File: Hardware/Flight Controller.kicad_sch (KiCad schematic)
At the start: 170 parts, among them J1 USB4110GFA, J2 ST_LINK, J3 4in1 ESC, J4 FPV, J5 GPS, J6 RC Receiver, Q1 AO3407A, SW1 reset, SW2 SSSS810701, U1 TPS54302, U10 W25Q128JVSIQ, U11 STM32H743VITx, U12 BMI270, U2 AP63205WU, U3 AZ1117-3.3, U4 USBLC6-2SC6, U5 AT7456E, U6 INA226, U7 ICM-42688-P, U8 QMC5883P, U9 BMP388, Y1 27Mhz 20pF, Y2 8MHz 12pF

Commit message: Added connectors STEP files, edited Schematics and started layout
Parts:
- added C15: 0.1uF, Capacitor_SMD:C_0402_1005Metric, symbol Device:C_Small
- C7: footprint Capacitor_SMD:C_0603_1608Metric -> Capacitor_SMD:C_0805_2012Metric
- J2: footprint Connector_PinHeader_2.54mm:PinHeader_1x04_P2.54mm_Horizontal -> memo:CONN-SMD_4P-P1.00_SM04B-SRSS-TB-LF-SN
- J4: footprint Connector_JST:JST_SH_SM04B-SRSS-TB_1x04-1MP_P1.00mm_Horizontal -> memo:CONN-SMD_4P-P1.00_SM04B-SRSS-TB-LF-SN
- J6: footprint Connector_JST:JST_GH_SM04B-GHS-TB_1x04-1MP_P1.25mm_Horizontal -> memo:CONN-SMD_4P-P1.00_SM04B-SRSS-TB-LF-SN
- R7: value 1k -> 330
- TP21, TP26: footprint Solderpoint:Solderpad -> Solderpoint:BAT pad
- renumbered C15 to C16, C16 to C17, C17 to C18, C18 to C19, C19 to C20, C20 to C21, C21 to C22, C22 to C23, C23 to C24, C24 to C25, C25 to C26, C26 to C27, C27 to C28, C28 to C29, C29 to C30, C30 to C31, C31 to C32, C32 to C33, C33 to C34, C34 to C35, C35 to C36, C36 to C37, C37 to C38, C38 to C39, C39 to C40, C40 to C41, C41 to C42, C42 to C43, C43 to C44, C44 to C45, C45 to C46, C46 to C47, C47 to C48, C48 to C49, C49 to C50, C50 to C51, C51 to C52, C52 to C53, C53 to C54, C54 to C55, C55 to C56
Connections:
- net +5V_USB: now also C15.1
- net GND: now also C15.2
- net A5: now reaches J1.A5 (CC1), R1.2
- net B5: now reaches J1.B5 (CC2), R2.2
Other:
- moved on the sheet: R7

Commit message: This commits updates BOM for Test Board, Changes the Ferrit bead value
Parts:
- FB1: value 120r @ 100KHz -> 1k@100Mhz
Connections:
- net M5: now also J3.6 (Pin_6); no longer J3.3 (Pin_3)
- net M6: now also J3.5 (Pin_5); no longer J3.4 (Pin_4)
- net M7: now also J3.4 (Pin_4); no longer J3.5 (Pin_5)
- net M8: now also J3.3 (Pin_3); no longer J3.6 (Pin_6)
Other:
- moved on the sheet: C13, C14
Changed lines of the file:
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@@
 	(wire
 		(pts
-			(xy 105.41 157.48) (xy 105.41 163.83)
+			(xy 105.41 157.48) (xy 105.41 161.29)
 		)
 		(stroke
@@
 	(wire
 		(pts
-			(xy 110.49 157.48) (xy 110.49 163.83)
+			(xy 110.49 157.48) (xy 110.49 161.29)
 		)
 		(stroke
@@
 	(wire
 		(pts
-			(xy 110.49 168.91) (xy 110.49 171.45)
+			(xy 110.49 166.37) (xy 110.49 171.45)
 		)
 		(stroke
@@
 	(wire
 		(pts
-			(xy 105.41 168.91) (xy 105.41 171.45)
+			(xy 105.41 166.37) (xy 105.41 171.45)
 		)
 		(stroke
@@
 		)
 	)
+	(label "FB_5V"
+		(at 91.44 160.02 0)
+		(effects
+			(font
+				(size 0.762 0.762)
+			)
+			(justify left bottom)
+		)
+	)
 	(label "reset"
 		(at 163.83 210.82 0)
@@
 		)
 	)
-	(global_label "QMC_SDA"
+	(global_label "M8"
 		(shape input)
-		(at 284.48 212.09 270)
+		(at 605.79 181.61 0)
 		(fields_autoplaced yes)
 		(effects
 			(font
 				(size 0.762 0.762)
+				(thickness 0.1524)
+				(bold yes)
 			)
-			(justify right)
+			(justify left)
 		)
 		(property "Intersheetrefs" "${INTERSHEET_REFS}"
-			(at 284.48 219.034 90)
+			(at 609.4635 181.61 0)
 			(effects
 				(font
 					(size 1.27 1.27)
 				)
-				(justify right)
+				(justify left)
 				(hide yes)
 			)
 		)
 	)
-	(global_label "M7"
+	(global_label "QMC_SDA"
 		(shape input)
-		(at 605.79 186.69 0)
+		(at 284.48 212.09 270)
 		(fields_autoplaced yes)
 		(effects
 			(font
 				(size 0.762 0.762)
-				(thickness 0.1524)
-				(bold yes)
 			)
-			(justify left)
+			(justify right)
 		)
 		(property "Intersheetrefs" "${INTERSHEET_REFS}"
-			(at 609.4635 186.69 0)
+			(at 284.48 219.034 90)
 			(effects
 				(font
 					(size 1.27 1.27)
 				)
-				(justify left)
+				(justify right)
 				(hide yes)
 			)
@@
 		)
 	)
-	(global_label "M5"
-		(shape input)
-		(at 605.79 181.61 0)
-		(fields_autoplaced yes)
-		(effects
-			(font
-				(size 0.762 0.762)
-				(thickness 0.1524)
-				(bold yes)
-			)
-			(justify left)
-		)
-		(property "Intersheetrefs" "${INTERSHEET_REFS}"
-			(at 609.4635 181.61 0)
-			(effects
-				(font
-					(size 1.27 1.27)
-				)
-				(justify left)
-				(hide yes)
-			)
-		)
-	)
 	(global_label "WIFI/RC_TX"
 		(shape input)
@@
 		)
 	)
+	(global_label "M6"
+		(shape input)
+		(at 605.79 186.69 0)
+		(fields_autoplaced yes)
+		(effects
+			(font
+				(size 0.762 0.762)
+				(thickness 0.1524)
+				(bold yes)
+			)
+			(justify left)
+		)
+		(property "Intersheetrefs" "${INTERSHEET_REFS}"
+			(at 609.4635 186.69 0)
+			(effects
+				(font
+					(size 1.27 1.27)
+				)
+				(justify left)
+				(hide yes)
+			)
+		)
+	)
+	(global_label "M7"
+		(shape input)
+		(at 605.79 184.15 0)
+		(fields_autoplaced yes)
+		(effects
+			(font
+				(size 0.762 0.762)
+				(thickness 0.1524)
+				(bold yes)
+			)
+			(justify left)
+		)
+		(property "Intersheetrefs" "${INTERSHEET_REFS}"
+			(at 609.4635 184.15 0)
+			(effects
+				(font
+					(size 1.27 1.27)
+				)
+				(justify left)
+				(hide yes)
+			)
+		)
+	)
 	(global_label "NRST"
 		(shape input)
@@
 		)
 	)
-	(global_label "M8"
-		(shape input)
-		(at 605.79 189.23 0)
-		(fields_autoplaced yes)
-		(effects
-			(font
-				(size 0.762 0.762)
-				(thickness 0.1524)
-				(bold yes)
-			)
-			(justify left)
-		)
-		(property "Intersheetrefs" "${INTERSHEET_REFS}"
-			(at 609.4635 189.23 0)
-			(effects
-				(font
-					(size 1.27 1.27)
-				)
-				(justify left)
-				(hide yes)
-			)
-		)
-	)
 	(global_label "ST_SWCLK"
 		(shape input)
@@
 		)
 	)
-	(global_label "M6"
-		(shape input)
-		(at 605.79 184.15 0)
-		(fields_autoplaced yes)
-		(effects
-			(font
-				(size 0.762 0.762)
-				(thickness 0.1524)
-				(bold yes)
-			)
-			(justify left)
-		)
-		(property "Intersheetrefs" "${INTERSHEET_REFS}"
-			(at 609.4635 184.15 0)
-			(effects
-				(font
-					(size 1.27 1.27)
-				)
-				(justify left)
-				(hide yes)
-			)
-		)
-	)
 	(global_label "GPS_TX"
 		(shape input)
@@
 		)
 	)
+	(global_label "M5"
+		(shape input)
+		(at 605.79 189.23 0)
+		(fields_autoplaced yes)
+		(effects
+			(font
+				(size 0.762 0.762)
+				(thickness 0.1524)
+				(bold yes)
+			)
+			(justify left)
+		)
+		(property "Intersheetrefs" "${INTERSHEET_REFS}"
+			(at 609.4635 189.23 0)
+			(effects
+				(font
+					(size 1.27 1.27)
+				)
+				(justify left)
+				(hide yes)
+			)
+		)
+	)
 	(global_label "INA226_ALERT"
 		(shape input)
@@
 	(symbol
 		(lib_id "Device:C_Small")
-		(at 110.49 166.37 180)
+		(at 110.49 163.83 180)
 		(unit 1)
 		(exclude_from_sim no)
@@
 		(dnp no)
 		(property "Reference" "C14"
-			(at 112.268 162.306 0)
+			(at 112.268 159.766 0)
 			(effects
 				(font
@@
 		)
 		(property "Value" "22uF"
-			(at 112.268 164.846 0)
+			(at 112.268 162.306 0)
 			(effects
 				(font
@@
 		)
 		(property "Footprint" "Capacitor_SMD:C_0603_1608Metric"
-			(at 110.49 166.37 0)
+			(at 110.49 163.83 0)
 			(effects
 				(font
@@
 		)
 		(property "Datasheet" "~"
-			(at 110.49 166.37 0)
+			(at 110.49 163.83 0)
 			(effects
 				(font
@@
 		)
 		(property "Description" "Unpolarized capacitor, small symbol"
-			(at 110.49 166.37 0)
+			(at 110.49 163.83 0)
 			(effects
 				(font
@@
 			)
 		)
-		(property "Value" "120r @ 100KHz"
+		(property "Value" "1k@100Mhz"
 			(at 480.0219 86.36 90)
 			(effects
@@
 	(symbol
 		(lib_id "Device:C_Small")
-		(at 105.41 166.37 180)
+		(at 105.41 163.83 180)
 		(unit 1)
 		(exclude_from_sim no)
@@
 		(dnp no)
 		(property "Reference" "C13"
-			(at 99.822 162.306 0)
+			(at 99.822 159.766 0)
 			(effects
 				(font
@@
 		)
 		(property "Value" "22uF"
-			(at 99.822 164.846 0)
+			(at 99.822 162.306 0)
 			(effects
 				(font
@@
 		)
 		(property "Footprint" "Capacitor_SMD:C_0603_1608Metric"
-			(at 105.41 166.37 0)
+			(at 105.41 163.83 0)
 			(effects
 				(font
@@
 		)
 		(property "Datasheet" "~"
-			(at 105.41 166.37 0)
+			(at 105.41 163.83 0)
 			(effects
 				(font
@@
 		)
 		(property "Description" "Unpolarized capacitor, small symbol"
-			(at 105.41 166.37 0)
+			(at 105.41 163.83 0)
 			(effects
 				(font

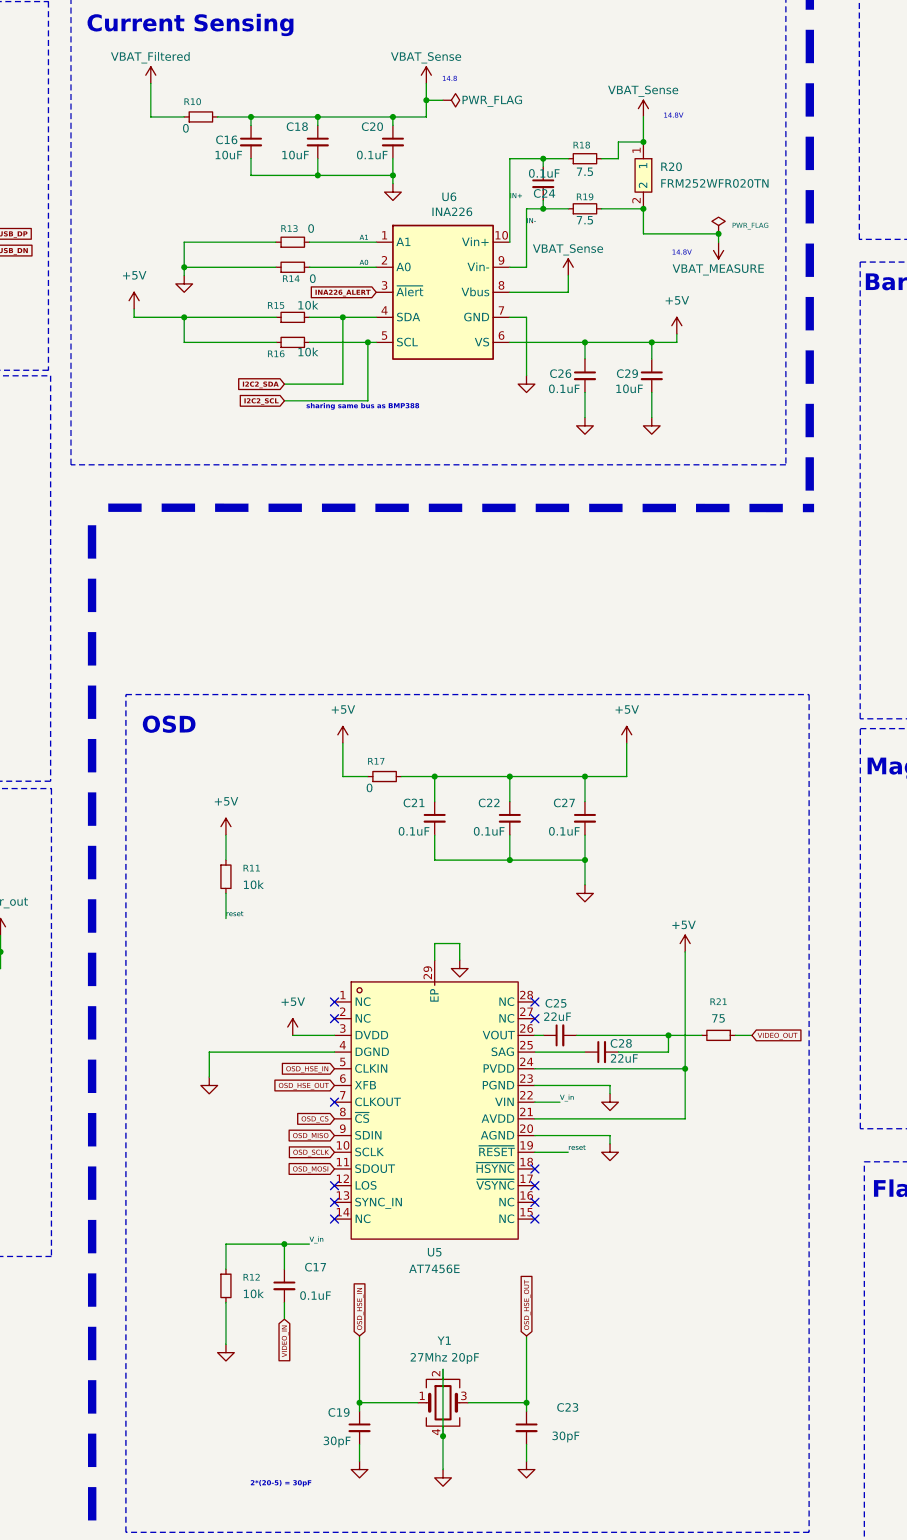
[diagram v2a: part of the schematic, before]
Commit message: Fixed Peripherals for OSD
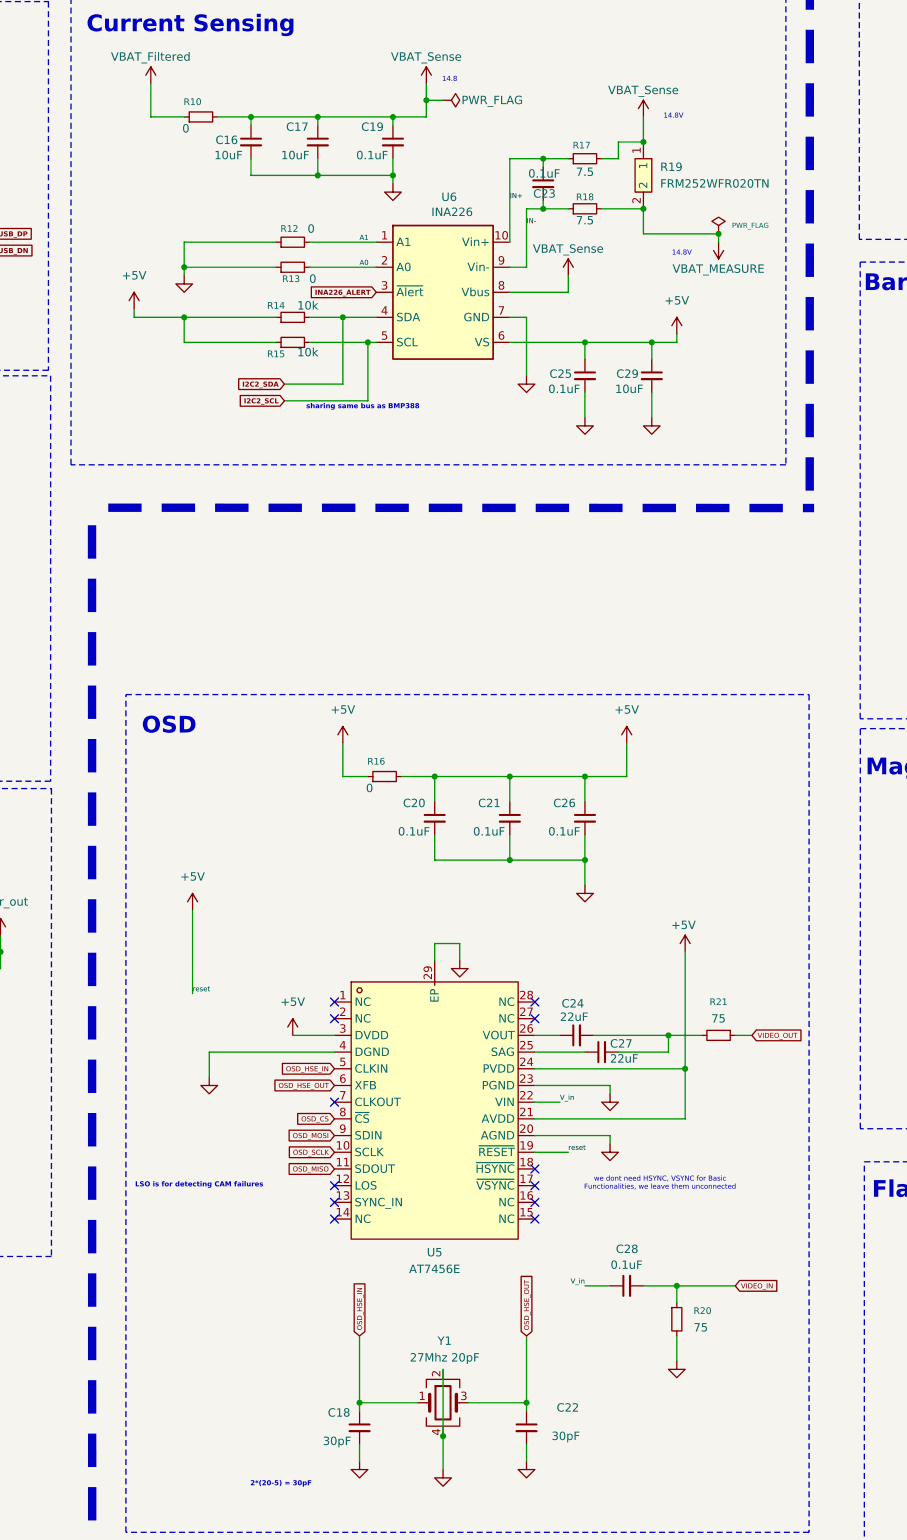
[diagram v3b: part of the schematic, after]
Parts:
- removed R11: 10k, Resistor_SMD:R_0402_1005Metric, symbol Device:R_Small
- R20: renamed from R12; value 10k -> 75
- renumbered C18 to C17, C19 to C18, C20 to C19, C21 to C20, C22 to C21, C23 to C22, C24 to C23, C25 to C24, C26 to C25, C27 to C26, C28 to C27, C17 to C28, R13 to R12, R14 to R13, R15 to R14, R16 to R15, R17 to R16, R18 to R17, R19 to R18, R20 to R19
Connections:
- net reset is gone; now on net +5V: R28.2, U10.7 (/HOLD/RESET(IO3)), U5.19 (~{RESET})
- net OSD_MISO: now also U5.11 (SDOUT); no longer U5.9 (SDIN)
- net OSD_MOSI: now also U5.9 (SDIN); no longer U5.11 (SDOUT)
- net VIDEO_IN: now also R20.1
- net V_in: no longer R20.1
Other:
- note added: "LSO is for detecting CAM failures"
- note added: "we dont need HSYNC, VSYNC for Basic Functionalities, we leave them unconnected"
- moved on the sheet: C24, C28, R20

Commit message: modified shcematics BOOT botton, added connector for VTX, did rough Layout
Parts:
- removed SW2: SSSS810701, memo:SW-SMD_SSSS810701, symbol switch-mine:SSSS810701
- added J7: VTX, memo:CONN-SMD_4P-P1.00_SM04B-SRSS-TB-LF-SN, symbol Connector_Generic:Conn_01x04
- added SW2: Boot, Button_Switch_SMD:SW_Push_SPST_NO_Alps_SKRK, symbol Switch:SW_Push
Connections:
- net +3.3V: now also SW2.1
- net +5V: no longer R28.2, U10.7 (/HOLD/RESET(IO3))
- net +pwr_out: now also J7.1 (Pin_1)
- net BOOT: now also SW2.2
- net GND: now also R33.1, J7.4 (Pin_4)
- net VIDEO_OUT: now also J7.2 (Pin_2)
- net VTX_TX: now also J7.3 (Pin_3)
- net vcap1: now reaches C40.2, U11.73 (VCAP)
- net sag: now reaches C27.1, U5.25 (SAG)
- net vout: now reaches C24.2, C27.2, R21.2
- net vcap2: now reaches C39.2, U11.48 (VCAP)
- new net reset_flash: R28.2, U10.7 (/HOLD/RESET(IO3))
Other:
- note added: "Second IMU"
- note removed: "Backup IMU"
- moved on the sheet: C42, C48, D5, D6, R30, R31, R33, U12

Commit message: changed into 2 LDO's one for the IMU's and one for the rest
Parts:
- removed U3: AZ1117-3.3, Package_TO_SOT_SMD:SOT-223, symbol Regulator_Linear:AZ1117-3.3
- added C57, C58: 0.1uF, Capacitor_SMD:C_0603_1608Metric, symbol Device:C_Small
- added D7: PMEG3020EH, Diode_SMD:D_SOD-123F, symbol Diode:PMEG3020EH
- added U13: XC6206PxxxMR, Package_TO_SOT_SMD:SOT-23-3, symbol Regulator_Linear:XC6206PxxxMR
- added U3: AP2112K-3.3, Package_TO_SOT_SMD:SOT-23-5, symbol Regulator_Linear:AP2112K-3.3
- C10: value 22uF -> 1uF
- C4: value 10uF -> 1uF
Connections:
- net +3.3V: now also U3.5 (VOUT); no longer C33.1, C35.1, C37.1, C42.1, U12.5 (VDDIO), U7.5 (VDDIO), U7.8 (VDD)
- net +5V: now also C58.1, D7.1 (K), U13.3 (VI), U3.1 (VIN), U3.3 (EN); no longer C13.2, C14.2, L2.2, R7.2, U2.1 (FB)
- net GND: now also C57.2, C58.2, U13.1 (GND), U3.2 (GND)
- new net +3V3_Sensors: C33.1, C35.1, C37.1, C42.1, C57.1, U12.5 (VDDIO), U13.2 (VO), U7.5 (VDDIO), U7.8 (VDD)
- new net +5V_REG: C13.2, C14.2, D7.2 (A), L2.2, R7.2, U2.1 (FB)
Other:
- note added: "IMU LDO"
- note added: "Main LDO"
- note removed: "LDO 5V -> 3.3V"
- moved on the sheet: C10, C4, D1, D3, R6

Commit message: Reformed the Schematics Files, reconfigured MCU pins
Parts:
- removed C1, C16, C17, C3: 10uF, Capacitor_SMD:C_0603_1608Metric, symbol Device:C_Small
- removed C10, C4, C45, C52: 1uF, Capacitor_SMD:C_0603_1608Metric, symbol Device:C_Small
- removed C11, C13, C14, C24, C27, C5, C9: 22uF, Capacitor_SMD:C_0603_1608Metric, symbol Device:C_Small
- removed C12: 75pF, Capacitor_SMD:C_0603_1608Metric, symbol Device:C_Small
- removed C15, C30, C31, C33, C34, C44, C46, C49, C51, C53, C56: 0.1uF, Capacitor_SMD:C_0402_1005Metric, symbol Device:C_Small
- removed C18, C22: 30pF, Capacitor_SMD:C_0603_1608Metric, symbol Device:C_Small
- removed C19, C2, C20, C21, C23, C25, C26, C28, C36, C38, C42, C43, C48, C50, C57, C58, C6, C8: 0.1uF, Capacitor_SMD:C_0603_1608Metric, symbol Device:C_Small
- removed C29: 10uF, Capacitor_SMD:C_0805_2012Metric, symbol Device:C_Small
- removed C32, C41: 4.7uF, Capacitor_SMD:C_0603_1608Metric, symbol Device:C_Small
- removed C35, C39, C40: 2.2uF, Capacitor_SMD:C_0603_1608Metric, symbol Device:C_Small
- removed C37, C55: 10nF, Capacitor_SMD:C_0402_1005Metric, symbol Device:C_Small
- removed C47, C54: 27pF, Capacitor_SMD:C_0402_1005Metric, symbol Device:C_Small
- removed C7: 100uF, Capacitor_SMD:C_0805_2012Metric, symbol Device:C_Small
- removed D1, D7: PMEG3020EH, Diode_SMD:D_SOD-123F, symbol Diode:PMEG3020EH
- removed D2: SMF26A, Diode_SMD:D_SMF, symbol Diode:SMF26A
- removed D3, D4, D5, D6: LED, LED_SMD:LED_0402_1005Metric, symbol Device:LED
- removed FB1: 1k@100Mhz, Inductor_SMD:L_0603_1608Metric, symbol Device:FerriteBead_Small
- removed H1, H2, H3, H4: MountingHole, MountingHole:MountingHole_3.2mm_M3_Pad_Via, symbol Mechanical:MountingHole
- removed J1: USB4110GFA, memo:GCT_USB4110GFA, symbol USB-C:USB4110GFA
- removed J2: ST_LINK, memo:CONN-SMD_4P-P1.00_SM04B-SRSS-TB-LF-SN, symbol Connector_Generic:Conn_01x04
- removed J3: 4in1 ESC, Connector_JST:JST_SH_SM08B-SRSS-TB_1x08-1MP_P1.00mm_Horizontal, symbol Connector_Generic:Conn_01x08
- removed J4: FPV, memo:CONN-SMD_4P-P1.00_SM04B-SRSS-TB-LF-SN, symbol Connector_Generic:Conn_01x04
- removed J5: GPS, Connector_JST:JST_SH_SM06B-SRSS-TB_1x06-1MP_P1.00mm_Horizontal, symbol Connector_Generic:Conn_01x06
- removed J6: RC Receiver, memo:CONN-SMD_4P-P1.00_SM04B-SRSS-TB-LF-SN, symbol Connector_Generic:Conn_01x04
- removed J7: VTX, memo:CONN-SMD_4P-P1.00_SM04B-SRSS-TB-LF-SN, symbol Connector_Generic:Conn_01x04
- removed JP1: 9V/12V, Jumper:SolderJumper-3_P1.3mm_Open_RoundedPad1.0x1.5mm_NumberLabels, symbol Jumper:SolderJumper_3_Open
- removed L1: 15uH, memo:IND-SMD_L5.4-W5.2, symbol Device:L_Small
- removed L2: 4.7uH, memo:IND-SMD_L4.4-W4.2, symbol Device:L_Small
- removed Q1: AO3407A, memo:AO3407A, symbol AO3407A:AO3407A
- removed R1, R2: 5.1k, Resistor_SMD:R_0402_1005Metric, symbol Device:R_Small
- removed R10, R12, R13, R16, R23, R35, R5: 0, Resistor_SMD:R_0402_1005Metric, symbol Device:R_Small
- removed R14, R15, R27, R28, R29, R33, R34: 10k, Resistor_SMD:R_0402_1005Metric, symbol Device:R_Small
- removed R17, R18: 7.5, Resistor_SMD:R_0402_1005Metric, symbol Device:R_Small
- removed R19: FRM252WFR020TN, memo:R2512, symbol shunt:FRM252WFR020TN
- removed R20, R21: 75, Resistor_SMD:R_0402_1005Metric, symbol Device:R_Small
- removed R22, R24, R25, R26: 4.7k, Resistor_SMD:R_0402_1005Metric, symbol Device:R_Small
- removed R3: 511k, Resistor_SMD:R_0402_1005Metric, symbol Device:R_Small
- removed R30, R31, R32, R6, R7: 330, Resistor_SMD:R_0402_1005Metric, symbol Device:R_Small
- removed R4: 105k, Resistor_SMD:R_0402_1005Metric, symbol Device:R_Small
- removed R5B1: 7.15K, Resistor_SMD:R_0402_1005Metric, symbol Device:R_Small
- removed R5C1: 5.23k, Resistor_SMD:R_0402_1005Metric, symbol Device:R_Small
- removed R8: 49.9, Resistor_SMD:R_0402_1005Metric, symbol Device:R_Small
- removed R9: 100k, Resistor_SMD:R_0402_1005Metric, symbol Device:R_Small
- removed SW1: reset, Button_Switch_SMD:SW_Push_SPST_NO_Alps_SKRK, symbol Switch:SW_Push
- removed SW2: Boot, Button_Switch_SMD:SW_Push_SPST_NO_Alps_SKRK, symbol Switch:SW_Push
- removed TP1, TP14, TP15, TP17, TP22, TP23, TP27, TP31, TP39, TP41, TP5, TP6, TP9: GND, Solderpoint:Solderpad, symbol Connector:TestPoint
- removed TP10: Motor 2, Solderpoint:Solderpad, symbol Connector:TestPoint
- removed TP11, TP3: 3.3V, Solderpoint:Solderpad, symbol Connector:TestPoint
- removed TP12, TP36, TP38, TP4, TP8: 5V, Solderpoint:Solderpad, symbol Connector:TestPoint
- removed TP13, TP16, TP19, TP7: servos, Solderpoint:Solderpad, symbol Connector:TestPoint
- removed TP18: Motor_3, Solderpoint:Solderpad, symbol Connector:TestPoint
- removed TP2: Motor 1, Solderpoint:Solderpad, symbol Connector:TestPoint
- removed TP20: 9V/12V, Solderpoint:Solderpad, symbol Connector:TestPoint
- removed TP21, TP26: GND, Solderpoint:BAT pad, symbol Connector:TestPoint
- removed TP24, TP33: VIDEO_OUT, Solderpoint:Solderpad, symbol Connector:TestPoint
- removed TP25: Motor_4, Solderpoint:Solderpad, symbol Connector:TestPoint
- removed TP28, TP32, TP34, TP37: GPS, Solderpoint:Solderpad, symbol Connector:TestPoint
- removed TP29: VTX_TX, Solderpoint:Solderpad, symbol Connector:TestPoint
- removed TP30: TELEMETRY_RX, Solderpoint:Solderpad, symbol Connector:TestPoint
- removed TP35: TELEMETRY_TX, Solderpoint:Solderpad, symbol Connector:TestPoint
- removed TP40: PWR, Solderpoint:Solderpad, symbol Connector:TestPoint
- removed U1: TPS54302, Package_TO_SOT_SMD:SOT-23-6, symbol Regulator_Switching:TPS54302
- removed U10: W25Q128JVSIQ, memo:W25Q128JVSIQ, symbol flash:W25Q128JVSIQ
- removed U11: STM32H743VITx, Package_QFP:LQFP-100_14x14mm_P0.5mm, symbol MCU_ST_STM32H7:STM32H743VITx
- removed U12: BMI270, memo:XDCR_BMI270, symbol bmi270:BMI270
- removed U13: XC6206PxxxMR, Package_TO_SOT_SMD:SOT-23-3, symbol Regulator_Linear:XC6206PxxxMR
- removed U2: AP63205WU, Package_TO_SOT_SMD:TSOT-23-6, symbol Regulator_Switching:AP63205WU
- removed U3: AP2112K-3.3, Package_TO_SOT_SMD:SOT-23-5, symbol Regulator_Linear:AP2112K-3.3
- removed U4: USBLC6-2SC6, Package_TO_SOT_SMD:SOT-23-6, symbol Power_Protection:USBLC6-2SC6
- removed U5: AT7456E, memo:AT7456E, symbol OSD:AT7456E
- removed U6: INA226, Package_SO:VSSOP-10_3x3mm_P0.5mm, symbol Sensor_Energy:INA226
- removed U7: ICM-42688-P, memo:PQFN50P300X250X97-14N, symbol ICM-42688:ICM-42688-P
- removed U8: QMC5883P, memo:QMC5883P, symbol Magneto:QMC5883P
- removed U9: BMP388, memo:PQFN50P200X200X80-10N, symbol BMP388:BMP388
- removed Y1: 27Mhz 20pF, Crystal:Crystal_SMD_3225-4Pin_3.2x2.5mm, symbol Device:Crystal_GND24
- removed Y2: 8MHz 12pF, Crystal:Crystal_SMD_3225-4Pin_3.2x2.5mm, symbol Device:Crystal_GND24
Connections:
- no-connect marks 60 -> 0
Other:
- added sheet Connectors (connectors.kicad_sch)
- added sheet MCU (MCU.kicad_sch)
- added sheet Power (power.kicad_sch)
- added sheet Sensors and Peripherals (Sensors.kicad_sch)
- note added: "8× motor outputs (PWM) 4× servo outputs (PWM) GPS + compass port (UART + I²C) RC receiver (SBUS / ELRS UART) Telemetry UART CAN bus (4-pin) Airspeed (I²C) VTX (analog + 9/12 V) DJI FPV (UART + SBUS) USB-C port"
- note added: "Airspeed and mag, yet to be picked"
- note added: "Comments"
- note added: "ICM-42688P (primary IMU) - SPI BMI270 (backup IMU) - SPI BMP388 barometer - I²C Magnetometer (IST8310 / LIS3MDL) - I²C Airspeed sensor (MS4525DO) - I²C AT7456E OSD - SPI W25Q128 flash memory (16 Mbit) - SPI CAN transceiver (SN65HVD230) - FDCAN"
- note added: "MCU: STM32H743VIT6 ARM Cortex-M7 @ 480 MHz 2 MB Flash, 1 MB RAM LQFP-100 Package Hardware floating-point unit (FPU) 16-bit/32-bit timers with PWM 4× SPI, 4× I2C, 8× USART/UART 2× FDCAN, USB OTG FS/HS 3× 16-bit ADC (up to 36 channels) DMA with DMAMUX Built-in UART signal inversion Operating voltage: 1.71V - 3.6V"
- note added: "Signal"
- note added: "TVS + reverse polarity protection Dual buck converters (5 V + 9/12 V) Dual LDO rails (3.3 V digital + 3.3 V sensors) USB-C power + automatic power switching Basic input filtering INA226 voltage/current monitor - I²"
- note removed: "12V or 9V switching regulator"
- note removed: "12V output"
- note removed: "14.8"
- note removed: "14.8V"
- note removed: "2*(20 - 5) = 30pF"
- note removed: "2*(20-5) = 30pF"
- note removed: "9V output"
- note removed: "Analog Filter"
- note removed: "Barometer"
- note removed: "Boot"
- note removed: "Connectors"
- note removed: "Current Sensing"
- note removed: "Debugger"
- note removed: "Debugging reasons, could be left unconnected"
- note removed: "Decoupling and bulk Filtering"
- note removed: "FPV 9/12V"
- note removed: "Flash Memory"
- note removed: "GPS"
- note removed: "HIGH = (0x77) address LOW = (0x76) address"
- note removed: "IMU"
- note removed: "IMU LDO"
- note removed: "LSO is for detecting CAM failures"
- note removed: "Lipo -> 5V"
- note removed: "MCU"
- note removed: "Magnetometer"
- note removed: "Main LDO"
- note removed: "Motors PWM pins"
- note removed: "OSD"
- note removed: "Power System"
- note removed: "Reset"
- note removed: "Second IMU"
- note removed: "Sensors and Peripherals"
- note removed: "TVS and reverse polarity protection"
- note removed: "Telemetry"
- note removed: "USB-C connection"
- note removed: "VTX"
- note removed: "enable pin max = 7V, V_out = V_in * (R2 / (R1 + R2)) V_out = 2.5V"
- note removed: "sharing same bus as BMP388"
- note removed: "sharing same bus as INA226"
- note removed: "to select i^2C protocol"
- note removed: "we dont need HSYNC, VSYNC for Basic Functionalities, we leave them unconnected"
